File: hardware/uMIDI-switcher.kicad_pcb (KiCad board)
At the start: 2 copper layers, 127 x 60 mm, 104 parts, among them Q1 BSS138, Q2 BSS138, Q3 BSS138, Q4 BSS138, Q5 BSS138, Q6 BSS138, Q7 BSS138, Q8 BSS138, U1 MC7809CD, U2 MC7809CD, U3 MC7809CD, U4 MC7809CD, X1 Jack_Stacked, X10 CONN_01X02, X11 CONN_01X02, X12 CONN_01X02, X13 uMIDI GPIO, X2 Jack_Stacked, X3 Jack_Stacked, X4 Jack_Stacked, X5 Jack_Stacked, X6 Jack_Stacked, X7 Jack_Stacked, X8 CONN_01X02, X9 uMIDI Power

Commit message: Assign net classes
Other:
- net class Audio Signal: clearance 0.4 -> 0.6; trace_width 0.4 -> 0.6
- net class Default: clearance 0.2 -> 0.3; trace_width 0.25 -> 0.3
- rule trace_clearance: 0.2 -> 0.3
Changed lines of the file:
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@@
 (kicad_pcb (version 4) (host pcbnew "(2015-09-12 BZR 6188)-product")
   (general
-    (links 276)
-    (no_connects 276)
-    (area 75.775 59.924999 208.0684 133.474044)
+    (links 274)
+    (no_connects 274)
+    (area 77.449999 68.949999 204.550001 129.050001)
     (thickness 1.6)
     (drawings 5)
@@
   )
   (setup
-    (last_trace_width 0.25)
-    (trace_clearance 0.2)
+    (last_trace_width 0.3)
+    (trace_clearance 0.3)
     (zone_clearance 0.508)
     (zone_45_only no)
@@
   (net 59 /Switch2/A)
   (net_class Default "This is the default net class."
-    (clearance 0.2)
-    (trace_width 0.25)
+    (clearance 0.3)
+    (trace_width 0.3)
     (via_dia 0.6)
     (via_drill 0.4)
@@
     (uvia_drill 0.1)
     (add_net /Looper1/Ctrl)
-    (add_net /Looper1/Loop_In)
-    (add_net "/Looper1/Single True Bypass/FX_Return")
-    (add_net "/Looper1/Single True Bypass/FX_Send")
-    (add_net "/Looper1/Single True Bypass/bypass")
     (add_net "/Looper1/Single True Bypass/relais_n")
     (add_net "/Looper1/Single True Bypass/relais_p")
     (add_net /Looper2/Ctrl)
-    (add_net /Looper2/Loop_In)
-    (add_net "/Looper2/Single True Bypass/FX_Return")
-    (add_net "/Looper2/Single True Bypass/FX_Send")
-    (add_net "/Looper2/Single True Bypass/bypass")
     (add_net "/Looper2/Single True Bypass/relais_n")
     (add_net "/Looper2/Single True Bypass/relais_p")
     (add_net /Looper3/Ctrl)
-    (add_net /Looper3/Loop_In)
-    (add_net "/Looper3/Single True Bypass/FX_Return")
-    (add_net "/Looper3/Single True Bypass/FX_Send")
-    (add_net "/Looper3/Single True Bypass/bypass")
     (add_net "/Looper3/Single True Bypass/relais_n")
     (add_net "/Looper3/Single True Bypass/relais_p")
     (add_net /Looper4/Ctrl)
-    (add_net /Looper4/Loop_In)
-    (add_net "/Looper4/Single True Bypass/FX_Return")
-    (add_net "/Looper4/Single True Bypass/FX_Send")
-    (add_net "/Looper4/Single True Bypass/bypass")
     (add_net "/Looper4/Single True Bypass/relais_n")
     (add_net "/Looper4/Single True Bypass/relais_p")
     (add_net /Looper5/Ctrl)
-    (add_net /Looper5/Loop_In)
-    (add_net /Looper5/Loop_Out)
-    (add_net "/Looper5/Single True Bypass/FX_Return")
-    (add_net "/Looper5/Single True Bypass/FX_Send")
-    (add_net "/Looper5/Single True Bypass/bypass")
     (add_net "/Looper5/Single True Bypass/relais_n")
     (add_net "/Looper5/Single True Bypass/relais_p")
@@
     (add_net /Switch2/relais_p)
     (add_net /Tuner/Ctrl)
-    (add_net /Tuner/FX_Send)
-    (add_net /Tuner/Loop_In)
-    (add_net /Tuner/bypass)
     (add_net /Tuner/relais_n)
     (add_net /Tuner/relais_p)
@@
   )
   (net_class "Audio Signal" ""
-    (clearance 0.4)
-    (trace_width 0.4)
+    (clearance 0.6)
+    (trace_width 0.6)
     (via_dia 0.6)
     (via_drill 0.4)
     (uvia_dia 0.3)
     (uvia_drill 0.1)
+    (add_net /Looper1/Loop_In)
+    (add_net "/Looper1/Single True Bypass/FX_Return")
+    (add_net "/Looper1/Single True Bypass/FX_Send")
+    (add_net "/Looper1/Single True Bypass/bypass")
+    (add_net /Looper2/Loop_In)
+    (add_net "/Looper2/Single True Bypass/FX_Return")
+    (add_net "/Looper2/Single True Bypass/FX_Send")
+    (add_net "/Looper2/Single True Bypass/bypass")
+    (add_net /Looper3/Loop_In)
+    (add_net "/Looper3/Single True Bypass/FX_Return")
+    (add_net "/Looper3/Single True Bypass/FX_Send")
+    (add_net "/Looper3/Single True Bypass/bypass")
+    (add_net /Looper4/Loop_In)
+    (add_net "/Looper4/Single True Bypass/FX_Return")
+    (add_net "/Looper4/Single True Bypass/FX_Send")
+    (add_net "/Looper4/Single True Bypass/bypass")
+    (add_net /Looper5/Loop_In)
+    (add_net /Looper5/Loop_Out)
+    (add_net "/Looper5/Single True Bypass/FX_Return")
+    (add_net "/Looper5/Single True Bypass/FX_Send")
+    (add_net "/Looper5/Single True Bypass/bypass")
+    (add_net /Tuner/FX_Send)
+    (add_net /Tuner/Loop_In)
+    (add_net /Tuner/bypass)
     (add_net GNDA)
   )

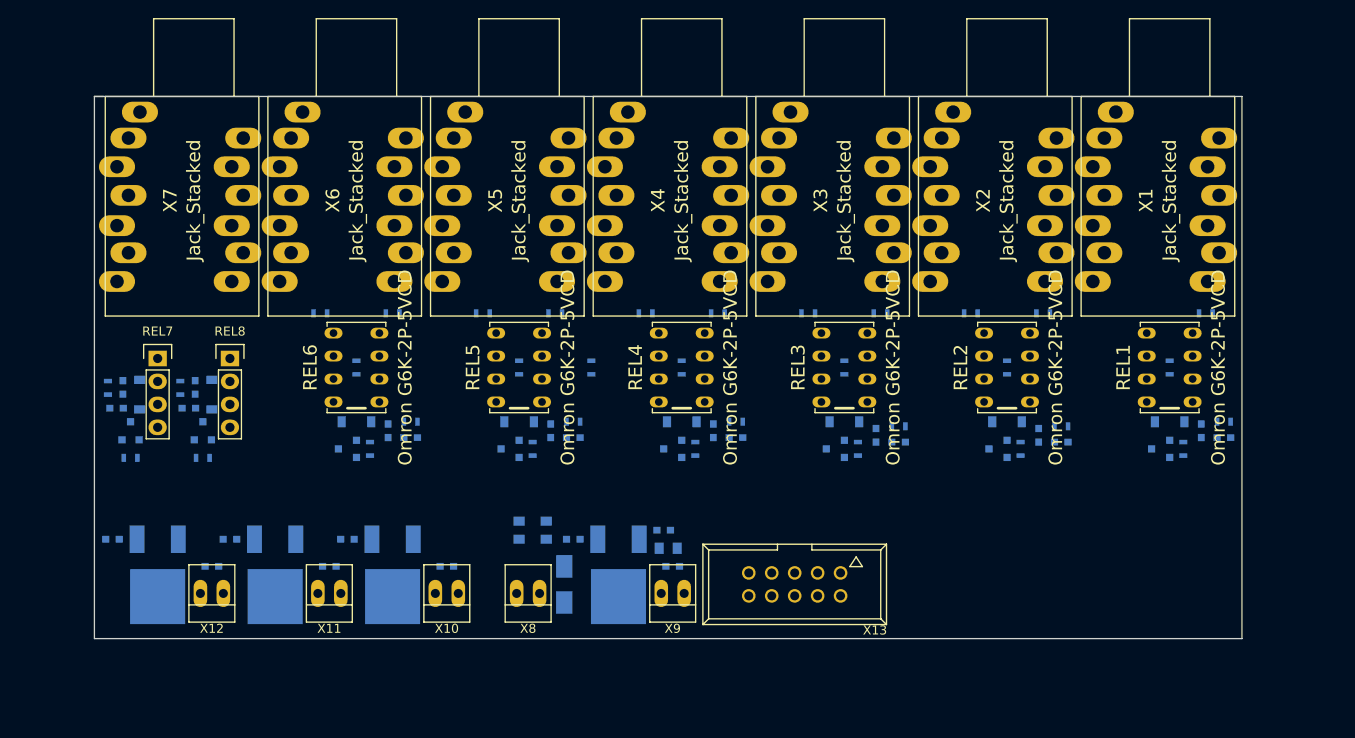
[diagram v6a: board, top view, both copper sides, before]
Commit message: Use two layers; Shrink placement
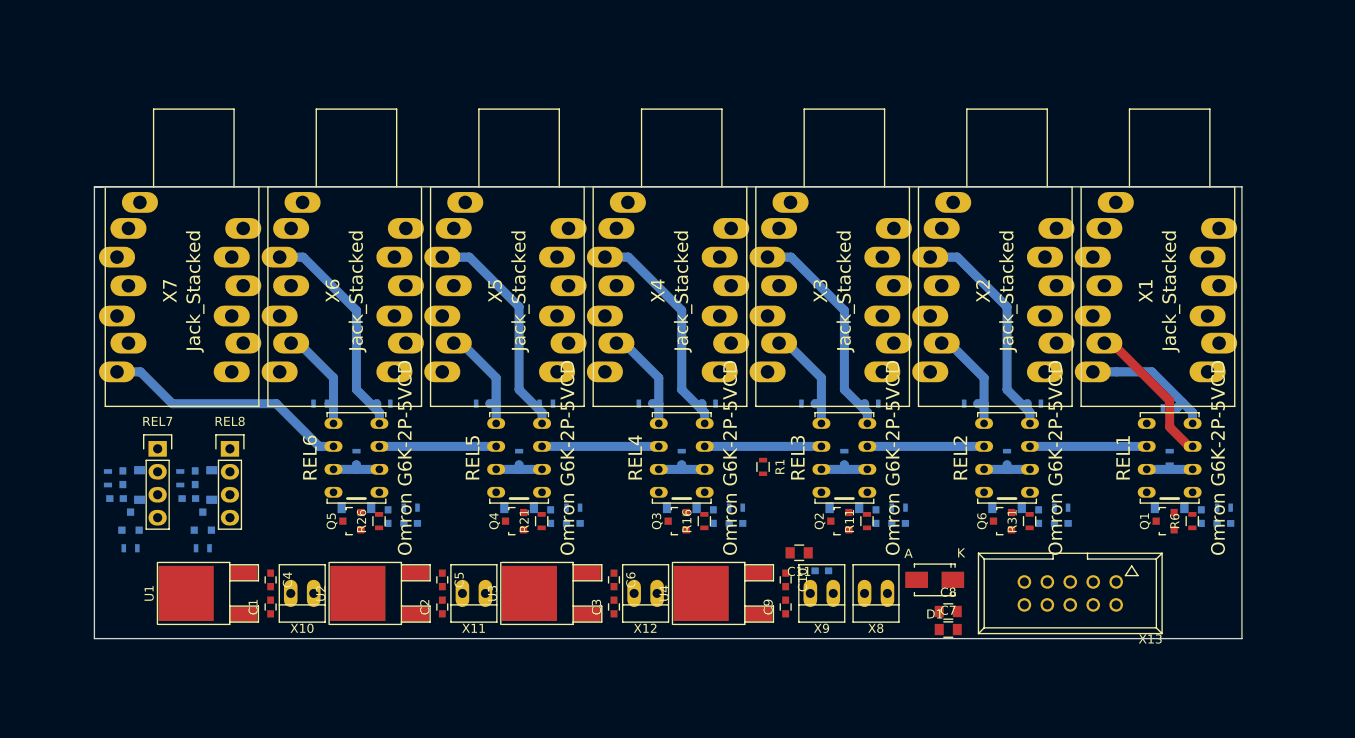
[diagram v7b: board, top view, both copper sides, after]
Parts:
- C1, C10, C11, C2, C3, C4, C5, C6, C7, C8, C9, D1, Q1, Q2, Q3, Q4, Q5, Q6, R1, R11, R16, R21, R26, R31, R6, U1, U2, U3, U4: moved to F.Cu
- moved C3 56.0 mm to (135.0, 125.5), turned to 90 degrees
- moved C8 48.3 mm to (172.0, 126.0), turned to 0 degrees
- moved X12 48.0 mm to (138.5, 124.0)
- moved U3 47.9 mm to (132.0, 124.0), turned to 90 degrees
- moved C7 45.8 mm to (172.0, 128.0), turned to 0 degrees
- moved C6 44.5 mm to (135.0, 122.5), turned to 270 degrees
- moved D1 41.0 mm to (170.5, 122.5), turned to 180 degrees
- moved X8 38.5 mm to (164.0, 124.0)
- moved X13 30.5 mm to (185.5, 124.0)
- moved C2 24.7 mm to (116.0, 125.5), turned to 90 degrees
- moved C9 24.7 mm to (154.0, 125.5), turned to 90 degrees
- moved R1 22.0 mm to (151.5, 110.0)
- moved C4 19.6 mm to (97.0, 122.5), turned to 270 degrees
- moved U1 17.6 mm to (94.0, 124.0), turned to 90 degrees
- moved U2 16.6 mm to (113.0, 124.0), turned to 90 degrees
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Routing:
- net /Looper4/Single True Bypass/FX_Send: track 0.00 -> 27.7 mm
- net /Looper5/Loop_Out: track 0.00 -> 27.4 mm
- net /Looper1/Single True Bypass/FX_Send: track 0.00 -> 25.9 mm
- net /Looper5/Single True Bypass/FX_Send: track 0.00 -> 25.6 mm
- net /Looper3/Single True Bypass/FX_Send: track 0.00 -> 25.6 mm
- net /Looper2/Single True Bypass/FX_Send: track 0.00 -> 25.6 mm
- net /Tuner/Loop_In: track 0.00 -> 16.2 mm
- net /Tuner/FX_Send: track 0.00 -> 15.0 mm
- net /Looper3/Loop_In: track 0.00 -> 12.9 mm
- net /Looper2/Loop_In: track 0.00 -> 12.9 mm
- net /Looper1/Loop_In: track 0.00 -> 12.9 mm
- net /Looper4/Loop_In: track 0.00 -> 12.9 mm
- net /Looper5/Loop_In: track 0.00 -> 12.9 mm
- net /Looper2/Single True Bypass/FX_Return: track 0.00 -> 12.1 mm
- net /Looper1/Single True Bypass/FX_Return: track 0.00 -> 12.1 mm
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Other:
- board size 127 x 60 mm -> 127 x 50 mm
- net class Audio Signal: trace_width 0.6 -> 1; via_dia 0.6 -> 0.61; via_drill 0.4 -> 0.31
- net class Default: via_dia 0.6 -> 0.61; via_drill 0.4 -> 0.31
- net class GNDA added: clearance 0.3, trace_width 0.3, via_dia 0.61, via_drill 0.31
- net class Power: clearance 0.4 -> 0.3; via_dia 0.6 -> 0.61; via_drill 0.4 -> 0.31
- rule via_min_drill: 0.3 -> 0.31
- rule via_min_size: 0.4 -> 0.61

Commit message: Route everything except GND(A)
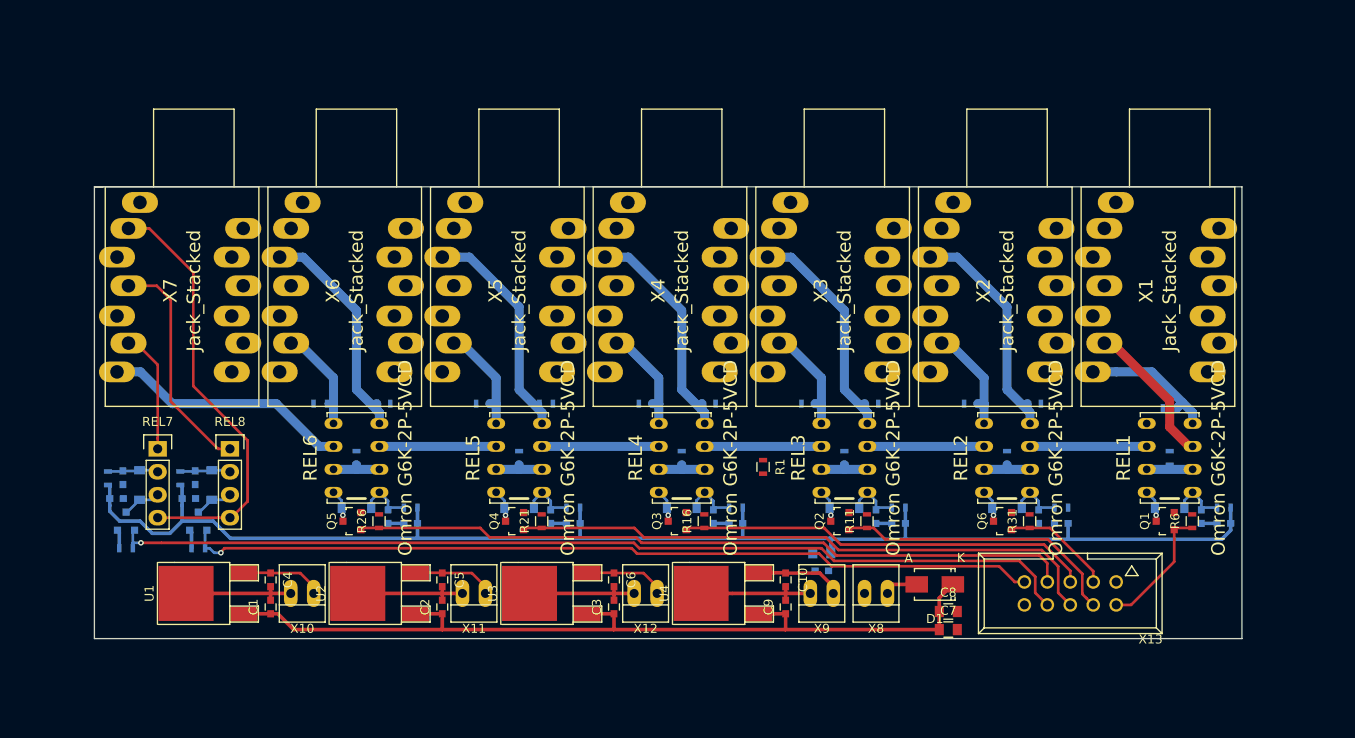
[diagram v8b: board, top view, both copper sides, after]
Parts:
- C11: moved to B.Cu
- moved C11 2.50 mm to (158.0, 119.5)
- moved D1 0.50 mm to (170.5, 123.0)
- moved Q7 0.50 mm to (81.0, 116.0)
- moved Q8 0.50 mm to (89.0, 116.0)
- moved R33 0.50 mm to (81.0, 119.0)
- moved R35 0.50 mm to (89.0, 119.0)
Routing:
- net +9V: track 0.00 -> 163.1 mm
- net /Switch1/Ctrl: track 0.00 -> 107.2 mm, vias 0 -> 1
- net +12V: track 0.00 -> 97.7 mm
- net /Switch2/Ctrl: track 0.00 -> 94.8 mm, vias 0 -> 1
- net /Looper5/Ctrl: track 0.00 -> 79.7 mm
- net /Looper4/Ctrl: track 0.00 -> 65.8 mm
- net GND: track 0.00 -> 65.7 mm
- net /Switch1/B: track 0.00 -> 47.7 mm
- net /Looper3/Ctrl: track 0.00 -> 45.8 mm
- net /Looper2/Ctrl: track 0.00 -> 32.0 mm
- net /Switch2/A: track 0.00 -> 25.3 mm
- net /Tuner/Ctrl: track 0.00 -> 14.0 mm
- net /Switch1/A: track 0.00 -> 13.5 mm
- net /Looper1/Ctrl: track 0.00 -> 12.3 mm
- net Net-(C6-Pad1): track 0.00 -> 9.16 mm
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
